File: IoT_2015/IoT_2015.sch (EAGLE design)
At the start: 9 parts

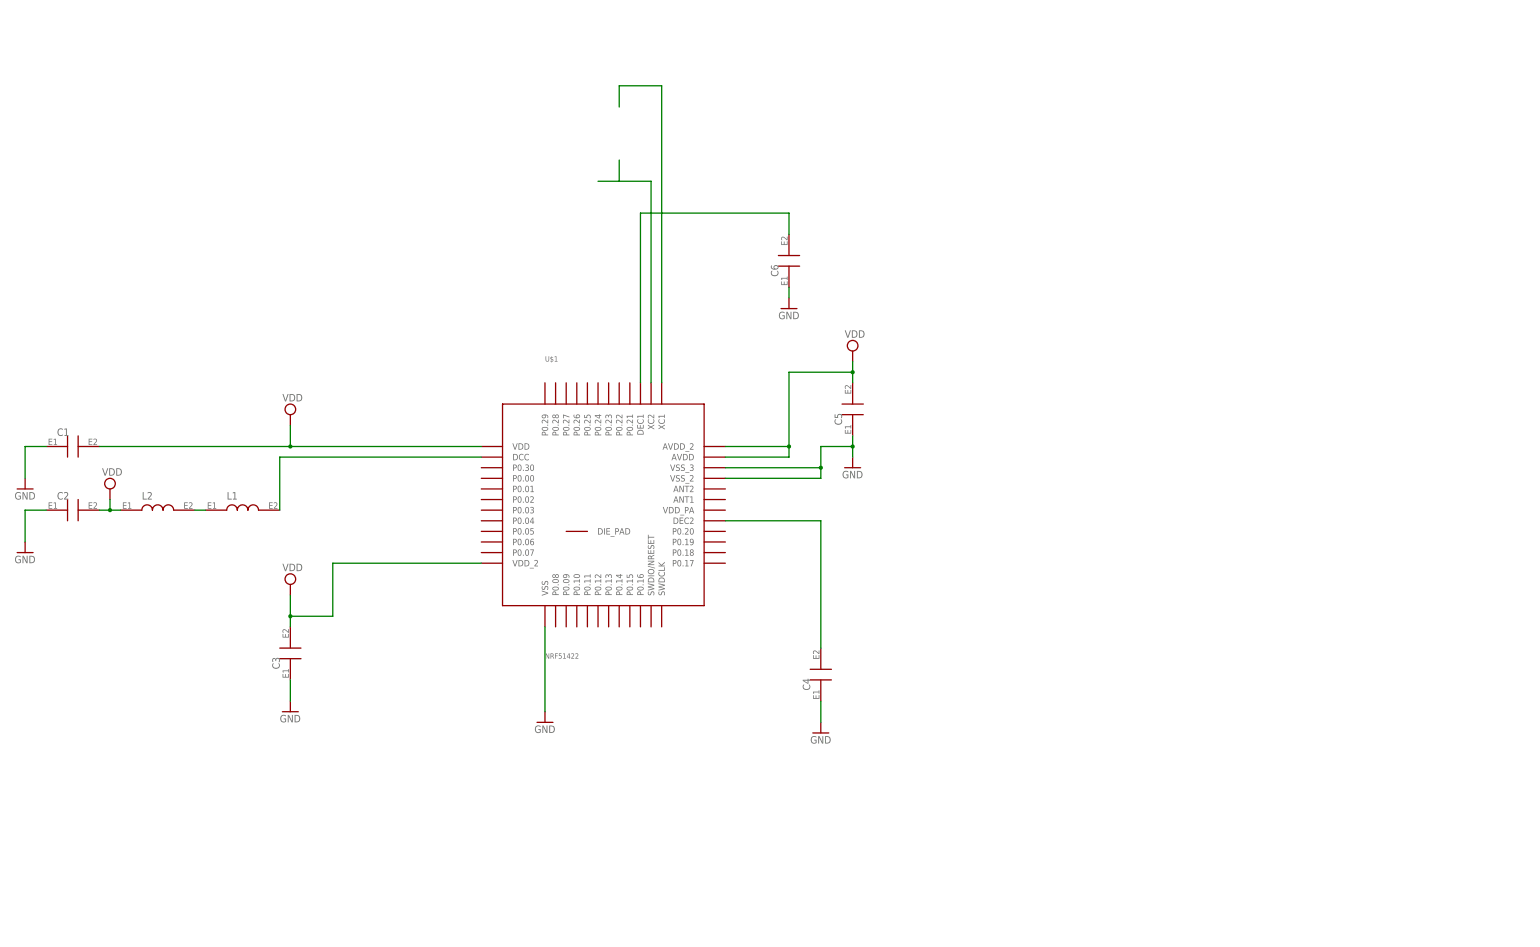
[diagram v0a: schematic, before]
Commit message: Refining
The 15Mhz crystal is replaced with footprint for 16Mhz crystal.
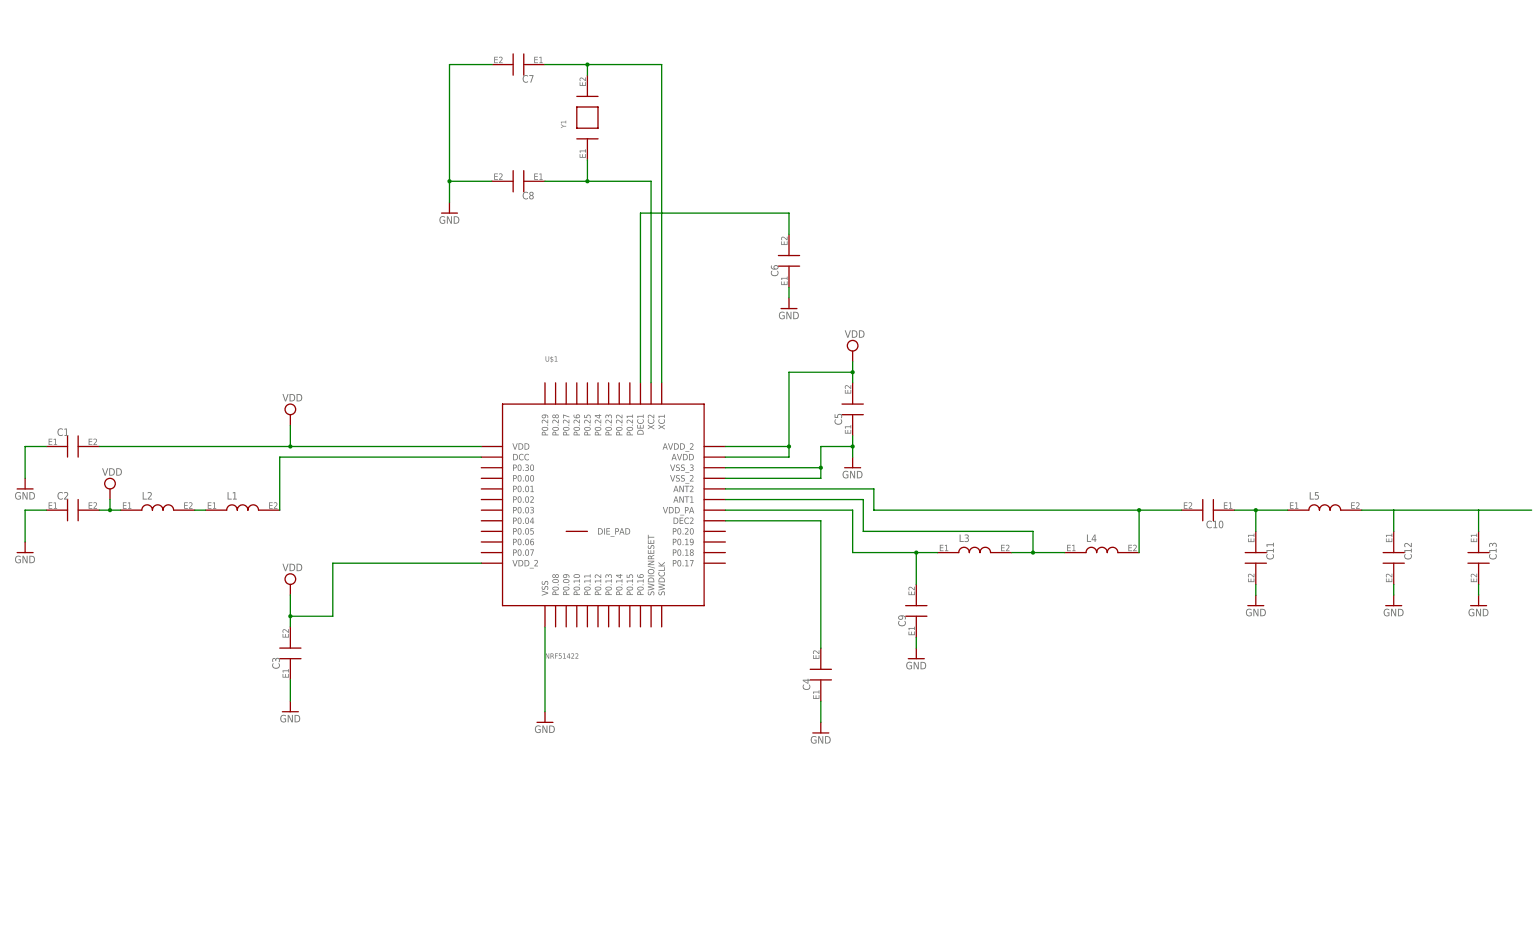
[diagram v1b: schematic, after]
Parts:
- added C10, C11, C12, C13, C7, C8, C9: (no value), Vishay:VJ1603_W1BC
- added L3, L4, L5: (no value), JohansonTechnology:JTI_CAT_2012_INDUCTORS_CHIP-242427
- added Y1: ABLS-16.000MHZ-B4-T, Abracon:ABLS-16.000MHZ-B4-T
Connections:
- new net N$11: C10.E1, C11.E1, L5.E1
- new net N$4: C12.E1, C13.E1, L5.E2
- new net N$5: C9.E2, L3.E1, U$1.VDD_PA
- new net N$6: L3.E2, L4.E1, U$1.ANT1
- new net N$7: C10.E2, L4.E2, U$1.ANT2
- net GND: now also C11.E2, C12.E2, C7.E2, C8.E2, C9.E1
- net N$10: now also C7.E1, Y1.E2
- net N$9: now also C8.E1, Y1.E1
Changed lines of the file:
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@@
 <part name="C6" library="Vishay" deviceset="VJ1603_W1BC" device=""/>
 <part name="GND7" library="supply1" deviceset="GND" device=""/>
+<part name="Y1" library="Abracon" deviceset="ABLS-16.000MHZ-B4-T" device=""/>
+<part name="C7" library="Vishay" deviceset="VJ1603_W1BC" device=""/>
+<part name="C8" library="Vishay" deviceset="VJ1603_W1BC" device=""/>
+<part name="GND8" library="supply1" deviceset="GND" device=""/>
+<part name="C9" library="Vishay" deviceset="VJ1603_W1BC" device=""/>
+<part name="GND9" library="supply1" deviceset="GND" device=""/>
+<part name="L3" library="JohansonTechnology" deviceset="JTI_CAT_2012_INDUCTORS_CHIP-242427" device=""/>
+<part name="L4" library="JohansonTechnology" deviceset="JTI_CAT_2012_INDUCTORS_CHIP-242427" device=""/>
+<part name="C10" library="Vishay" deviceset="VJ1603_W1BC" device=""/>
+<part name="C11" library="Vishay" deviceset="VJ1603_W1BC" device=""/>
+<part name="L5" library="JohansonTechnology" deviceset="JTI_CAT_2012_INDUCTORS_CHIP-242427" device=""/>
+<part name="C12" library="Vishay" deviceset="VJ1603_W1BC" device=""/>
+<part name="GND10" library="supply1" deviceset="GND" device=""/>
+<part name="GND11" library="supply1" deviceset="GND" device=""/>
+<part name="C13" library="Vishay" deviceset="VJ1603_W1BC" device=""/>
+<part name="GND12" library="supply1" deviceset="GND" device=""/>
 </parts>
 <sheets>
@@
 <instance part="C6" gate="G$1" x="142.24" y="104.14" rot="R90"/>
 <instance part="GND7" gate="1" x="142.24" y="93.98"/>
+<instance part="Y1" gate="G$1" x="93.98" y="139.7" rot="R90"/>
+<instance part="C7" gate="G$1" x="78.74" y="152.4" rot="R180"/>
+<instance part="C8" gate="G$1" x="78.74" y="124.46" rot="R180"/>
+<instance part="GND8" gate="1" x="60.96" y="116.84"/>
+<instance part="C9" gate="G$1" x="172.72" y="20.32" rot="R90"/>
+<instance part="GND9" gate="1" x="172.72" y="10.16"/>
+<instance part="L3" gate="G$1" x="185.42" y="35.56"/>
+<instance part="L4" gate="G$1" x="215.9" y="35.56"/>
+<instance part="C10" gate="G$1" x="243.84" y="45.72" rot="R180"/>
+<instance part="C11" gate="G$1" x="254" y="35.56" rot="R270"/>
+<instance part="L5" gate="G$1" x="269.24" y="45.72"/>
+<instance part="C12" gate="G$1" x="287.02" y="35.56" rot="R270"/>
+<instance part="GND10" gate="1" x="254" y="22.86" rot="MR0"/>
+<instance part="GND11" gate="1" x="287.02" y="22.86"/>
+<instance part="C13" gate="G$1" x="307.34" y="35.56" rot="R270"/>
+<instance part="GND12" gate="1" x="307.34" y="22.86"/>
 </instances>
 <busses>
@@
 <wire x1="142.24" y1="99.06" x2="142.24" y2="96.52" width="0.1524" layer="91"/>
 </segment>
+<segment>
+<pinref part="C7" gate="G$1" pin="E2"/>
+<wire x1="71.12" y1="152.4" x2="60.96" y2="152.4" width="0.1524" layer="91"/>
+<wire x1="60.96" y1="152.4" x2="60.96" y2="124.46" width="0.1524" layer="91"/>
+<pinref part="C8" gate="G$1" pin="E2"/>
+<wire x1="60.96" y1="124.46" x2="71.12" y2="124.46" width="0.1524" layer="91"/>
+<wire x1="60.96" y1="124.46" x2="60.96" y2="119.38" width="0.1524" layer="91"/>
+<junction x="60.96" y="124.46"/>
+<pinref part="GND8" gate="1" pin="GND"/>
+</segment>
+<segment>
+<pinref part="C9" gate="G$1" pin="E1"/>
+<pinref part="GND9" gate="1" pin="GND"/>
+<wire x1="172.72" y1="12.7" x2="172.72" y2="15.24" width="0.1524" layer="91"/>
+</segment>
+<segment>
+<pinref part="C12" gate="G$1" pin="E2"/>
+<pinref part="GND11" gate="1" pin="GND"/>
+<wire x1="287.02" y1="25.4" x2="287.02" y2="27.94" width="0.1524" layer="91"/>
+</segment>
+<segment>
+<pinref part="C11" gate="G$1" pin="E2"/>
+<pinref part="GND10" gate="1" pin="GND"/>
+<wire x1="254" y1="25.4" x2="254" y2="27.94" width="0.1524" layer="91"/>
+</segment>
+<segment>
+<wire x1="307.34" y1="25.4" x2="307.34" y2="27.94" width="0.1524" layer="91"/>
+</segment>
 </net>
 <net name="N$3" class="0">
@@
 <pinref part="U$1" gate="G$1" pin="XC2"/>
 <wire x1="109.22" y1="76.2" x2="109.22" y2="124.46" width="0.1524" layer="91"/>
-<wire x1="109.22" y1="124.46" x2="101.6" y2="124.46" width="0.1524" layer="91"/>
-<wire x1="101.6" y1="124.46" x2="96.52" y2="124.46" width="0.1524" layer="91"/>
-<wire x1="101.6" y1="124.46" x2="101.6" y2="129.54" width="0.1524" layer="91"/>
+<wire x1="109.22" y1="124.46" x2="93.98" y2="124.46" width="0.1524" layer="91"/>
+<pinref part="Y1" gate="G$1" pin="E1"/>
+<wire x1="93.98" y1="124.46" x2="93.98" y2="129.54" width="0.1524" layer="91"/>
+<pinref part="C8" gate="G$1" pin="E1"/>
+<wire x1="93.98" y1="124.46" x2="83.82" y2="124.46" width="0.1524" layer="91"/>
+<junction x="93.98" y="124.46"/>
 </segment>
 </net>
@@
 <segment>
 <pinref part="U$1" gate="G$1" pin="XC1"/>
-<wire x1="111.76" y1="76.2" x2="111.76" y2="147.32" width="0.1524" layer="91"/>
-<wire x1="111.76" y1="147.32" x2="101.6" y2="147.32" width="0.1524" layer="91"/>
-<wire x1="101.6" y1="147.32" x2="101.6" y2="142.24" width="0.1524" layer="91"/>
-</segment>
-</net>
+<wire x1="111.76" y1="76.2" x2="111.76" y2="152.4" width="0.1524" layer="91"/>
+<wire x1="111.76" y1="152.4" x2="93.98" y2="152.4" width="0.1524" layer="91"/>
+<pinref part="Y1" gate="G$1" pin="E2"/>
+<wire x1="93.98" y1="152.4" x2="93.98" y2="149.86" width="0.1524" layer="91"/>
+<pinref part="C7" gate="G$1" pin="E1"/>
+<wire x1="93.98" y1="152.4" x2="83.82" y2="152.4" width="0.1524" layer="91"/>
+<junction x="93.98" y="152.4"/>
+</segment>
+</net>
+<net name="N$5" class="0">
+<segment>
+<pinref part="U$1" gate="G$1" pin="VDD_PA"/>
+<wire x1="127" y1="45.72" x2="157.48" y2="45.72" width="0.1524" layer="91"/>
+<wire x1="157.48" y1="45.72" x2="157.48" y2="35.56" width="0.1524" layer="91"/>
+<wire x1="157.48" y1="35.56" x2="172.72" y2="35.56" width="0.1524" layer="91"/>
+<pinref part="C9" gate="G$1" pin="E2"/>
+<wire x1="172.72" y1="35.56" x2="172.72" y2="27.94" width="0.1524" layer="91"/>
+<pinref part="L3" gate="G$1" pin="E1"/>
+<wire x1="172.72" y1="35.56" x2="177.8" y2="35.56" width="0.1524" layer="91"/>
+<junction x="172.72" y="35.56"/>
+</segment>
+</net>
+<net name="N$6" class="0">
+<segment>
+<pinref part="L3" gate="G$1" pin="E2"/>
+<wire x1="195.58" y1="35.56" x2="200.66" y2="35.56" width="0.1524" layer="91"/>
+<wire x1="200.66" y1="35.56" x2="200.66" y2="40.64" width="0.1524" layer="91"/>
+<wire x1="200.66" y1="40.64" x2="160.02" y2="40.64" width="0.1524" layer="91"/>
+<wire x1="160.02" y1="40.64" x2="160.02" y2="48.26" width="0.1524" layer="91"/>
+<pinref part="U$1" gate="G$1" pin="ANT1"/>
+<wire x1="160.02" y1="48.26" x2="127" y2="48.26" width="0.1524" layer="91"/>
+<wire x1="200.66" y1="35.56" x2="208.28" y2="35.56" width="0.1524" layer="91"/>
+<pinref part="L4" gate="G$1" pin="E1"/>
+<junction x="200.66" y="35.56"/>
+</segment>
+</net>
+<net name="N$7" class="0">
+<segment>
+<pinref part="L4" gate="G$1" pin="E2"/>
+<wire x1="226.06" y1="35.56" x2="226.06" y2="45.72" width="0.1524" layer="91"/>
+<wire x1="226.06" y1="45.72" x2="162.56" y2="45.72" width="0.1524" layer="91"/>
+<wire x1="162.56" y1="45.72" x2="162.56" y2="50.8" width="0.1524" layer="91"/>
+<pinref part="U$1" gate="G$1" pin="ANT2"/>
+<wire x1="162.56" y1="50.8" x2="127" y2="50.8" width="0.1524" layer="91"/>
+<wire x1="226.06" y1="45.72" x2="236.22" y2="45.72" width="0.1524" layer="91"/>
+<pinref part="C10" gate="G$1" pin="E2"/>
+<junction x="226.06" y="45.72"/>
+</segment>
+</net>
+<net name="N$11" class="0">
+<segment>
+<pinref part="C10" gate="G$1" pin="E1"/>
+<wire x1="248.92" y1="45.72" x2="254" y2="45.72" width="0.1524" layer="91"/>
+<pinref part="C11" gate="G$1" pin="E1"/>
+<wire x1="254" y1="45.72" x2="254" y2="40.64" width="0.1524" layer="91"/>
+<pinref part="L5" gate="G$1" pin="E1"/>
+<wire x1="261.62" y1="45.72" x2="254" y2="45.72" width="0.1524" layer="91"/>
+<junction x="254" y="45.72"/>
+</segment>
+</net>
+<net name="N$4" class="0">
+<segment>
+<pinref part="L5" gate="G$1" pin="E2"/>
+<pinref part="C12" gate="G$1" pin="E1"/>
+<wire x1="279.4" y1="45.72" x2="287.02" y2="45.72" width="0.1524" layer="91"/>
+<wire x1="287.02" y1="45.72" x2="287.02" y2="40.64" width="0.1524" layer="91"/>
+<wire x1="287.02" y1="45.72" x2="307.34" y2="45.72" width="0.1524" layer="91"/>
+<pinref part="C13" gate="G$1" pin="E1"/>
+<wire x1="307.34" y1="45.72" x2="307.34" y2="40.64" width="0.1524" layer="91"/>
+<wire x1="307.34" y1="45.72" x2="320.04" y2="45.72" width="0.1524" layer="91"/>
+</segment>
+</net>

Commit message: Added sensor, battery and antenna to schematic
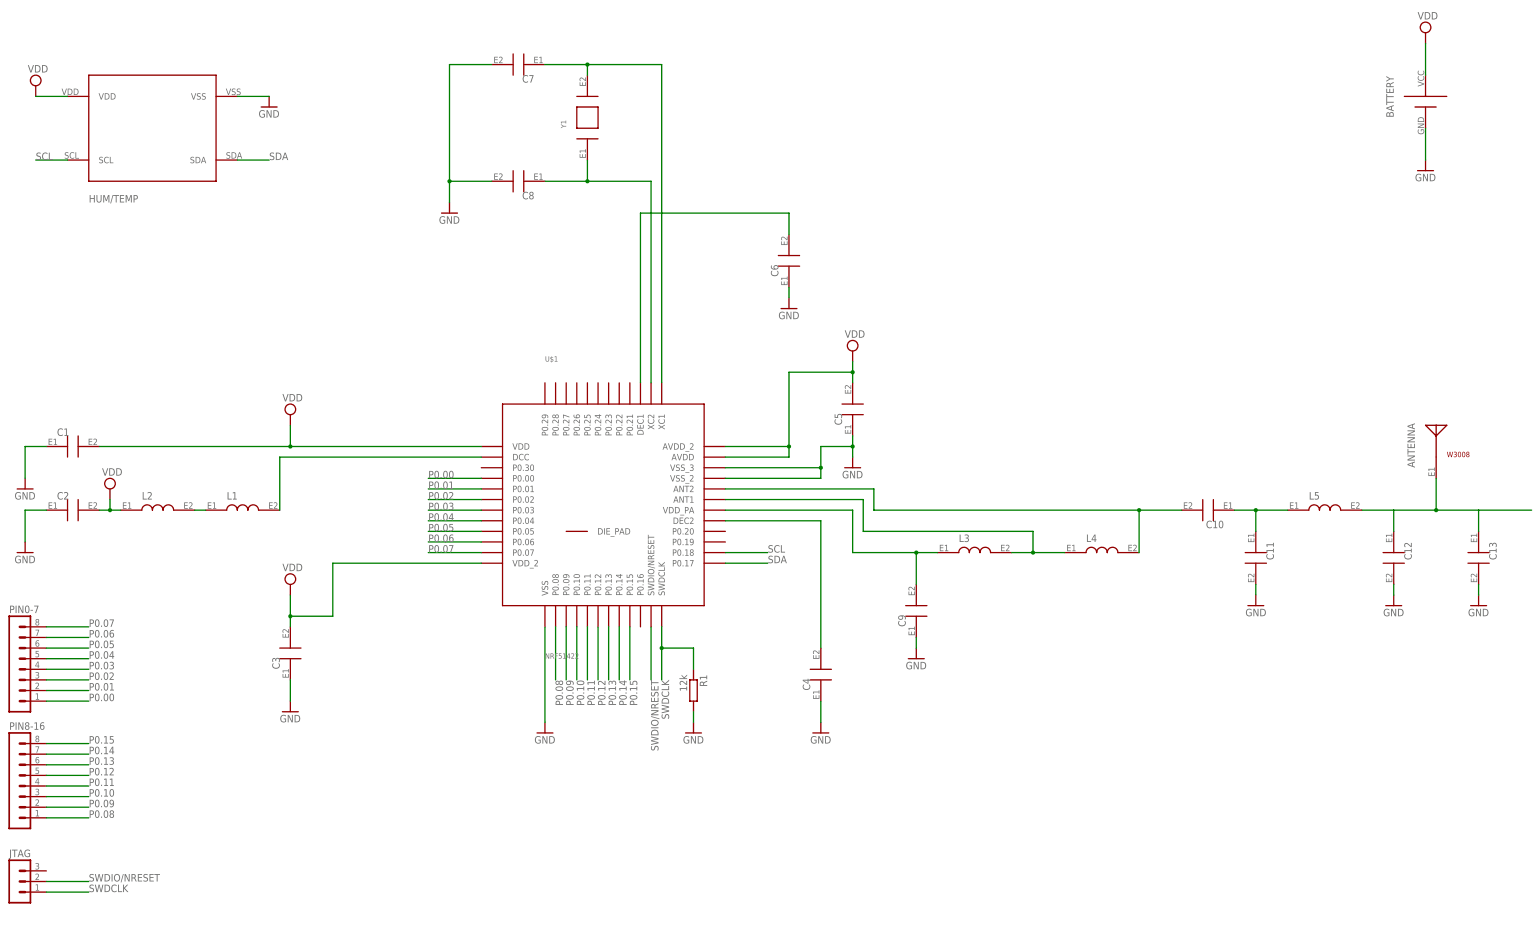
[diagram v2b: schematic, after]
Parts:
- added ANTENNA: W3008, Pulse:W3008
- added BATTERY: SMTU2032-G.TR, Renata:SMTU2032-G.TR
- added HUM/TEMP: SHTC1, Sensirion:SHTC1
- added JTAG: (no value), con-lstb:MA03-1
- added PIN0-7, PIN8-16: (no value), con-lstb:MA08-1
- added R1: 12k, resistor:R-EU_M0805
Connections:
- new net P0.00: PIN0-7.1, U$1.P0.00
- new net P0.01: PIN0-7.2, U$1.P0.01
- new net P0.02: PIN0-7.3, U$1.P0.02
- new net P0.03: PIN0-7.4, U$1.P0.03
- new net P0.04: PIN0-7.5, U$1.P0.04
- new net P0.05: PIN0-7.6, U$1.P0.05
- new net P0.06: PIN0-7.7, U$1.P0.06
- new net P0.07: PIN0-7.8, U$1.P0.07
- new net P0.08: PIN8-16.1, U$1.P0.08
- new net P0.09: PIN8-16.2, U$1.P0.09
- new net P0.10: PIN8-16.3, U$1.P0.10
- new net P0.11: PIN8-16.4, U$1.P0.11
- new net P0.12: PIN8-16.5, U$1.P0.12
- new net P0.13: PIN8-16.6, U$1.P0.13
- new net P0.14: PIN8-16.7, U$1.P0.14
- new net P0.15: PIN8-16.8, U$1.P0.15
- new net SCL: HUM/TEMP.SCL, U$1.P0.18
- new net SDA: HUM/TEMP.SDA, U$1.P0.17
- new net SWDCLK: JTAG.1, R1.1, U$1.SWDCLK
- new net SWDIO/NRESET: JTAG.2, U$1.SWDIO/NRESET
- net GND: now also BATTERY.GND, HUM/TEMP.VSS, R1.2
- net N$4: now also ANTENNA.E1
- net VDD: now also BATTERY.VCC, HUM/TEMP.VDD

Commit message: Finished the schematic
Refined the shematic with I2C-resistors for SDA and SCL, additional pins
for unused I/O:s.
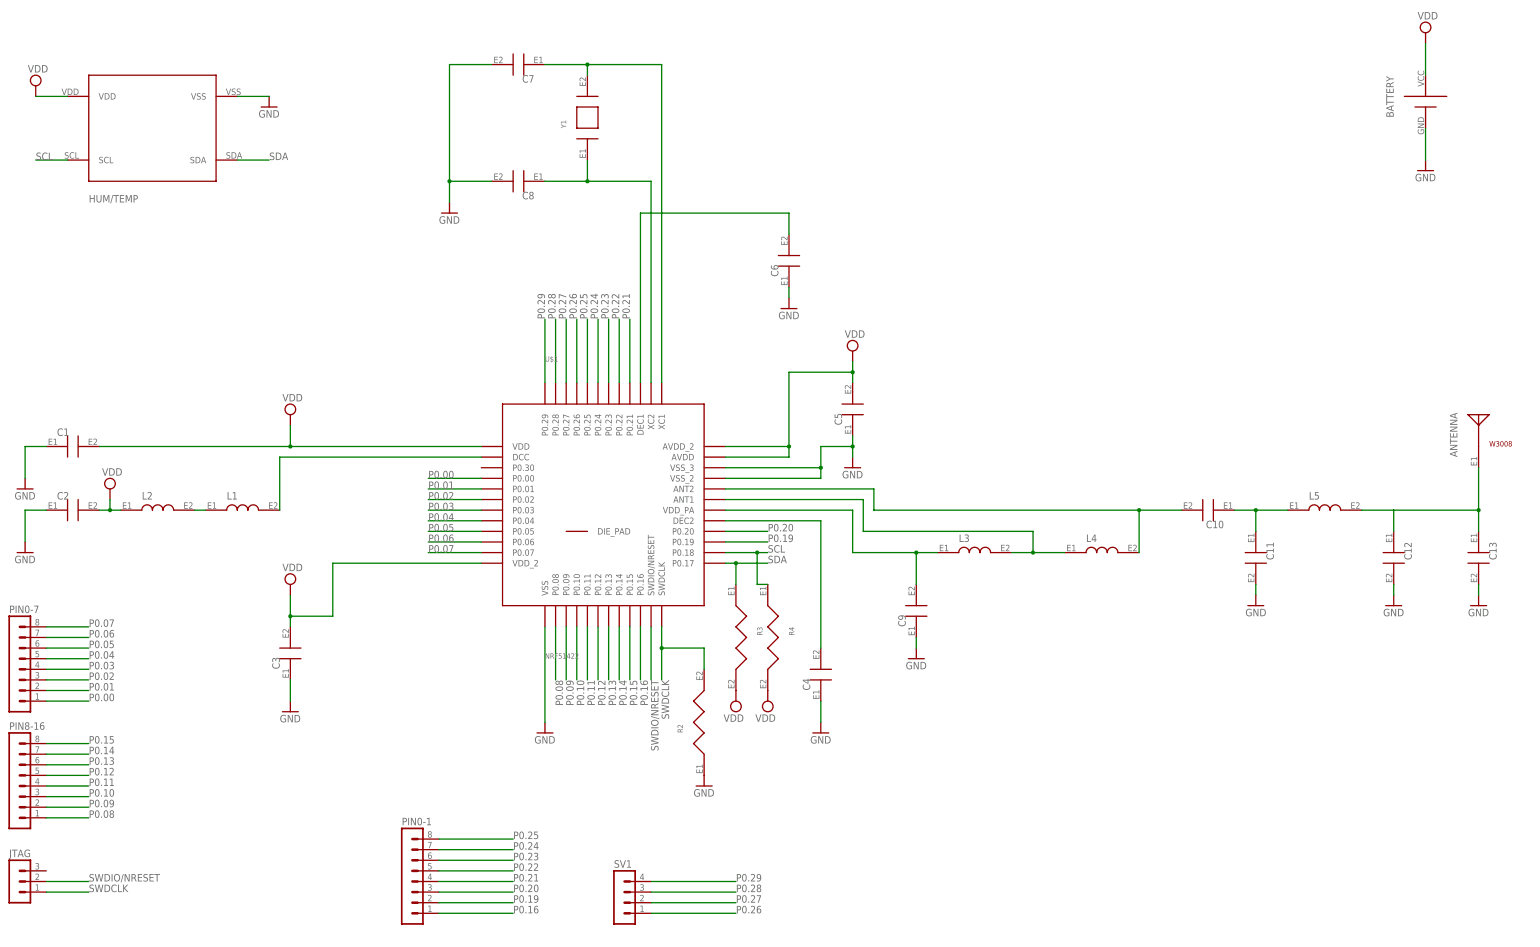
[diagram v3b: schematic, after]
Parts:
- removed R1: 12k, resistor:R-EU_M0805
- added PIN0-1: (no value), con-lstb:MA08-1
- added R2, R3, R4: (no value), Panasonic:ERJ-3GEYJ103V
- added SV1: (no value), con-lstb:MA04-1
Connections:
- new net P0.16: PIN0-1.1, U$1.P0.16
- new net P0.19: PIN0-1.2, U$1.P0.19
- new net P0.20: PIN0-1.3, U$1.P0.20
- new net P0.21: PIN0-1.4, U$1.P0.21
- new net P0.22: PIN0-1.5, U$1.P0.22
- new net P0.23: PIN0-1.6, U$1.P0.23
- new net P0.24: PIN0-1.7, U$1.P0.24
- new net P0.25: PIN0-1.8, U$1.P0.25
- new net P0.26: SV1.1, U$1.P0.26
- new net P0.27: SV1.2, U$1.P0.27
- new net P0.28: SV1.3, U$1.P0.28
- new net P0.29: SV1.4, U$1.P0.29
- net GND: now also R2.E1; no longer R1.2
- net SCL: now also R4.E1
- net SDA: now also R3.E1
- net SWDCLK: now also R2.E2; no longer R1.1
- net VDD: now also R3.E2, R4.E2
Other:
- moved on the sheet: ANTENNA
